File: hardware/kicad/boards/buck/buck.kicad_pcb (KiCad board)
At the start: 2 copper layers, 121 x 56 mm, 11 parts, among them J1 V1 ind (15V), J2 5V ud, J3 PWM (isoleret), J4 gate-forsyning, M1 IRF530N, U1 4N25

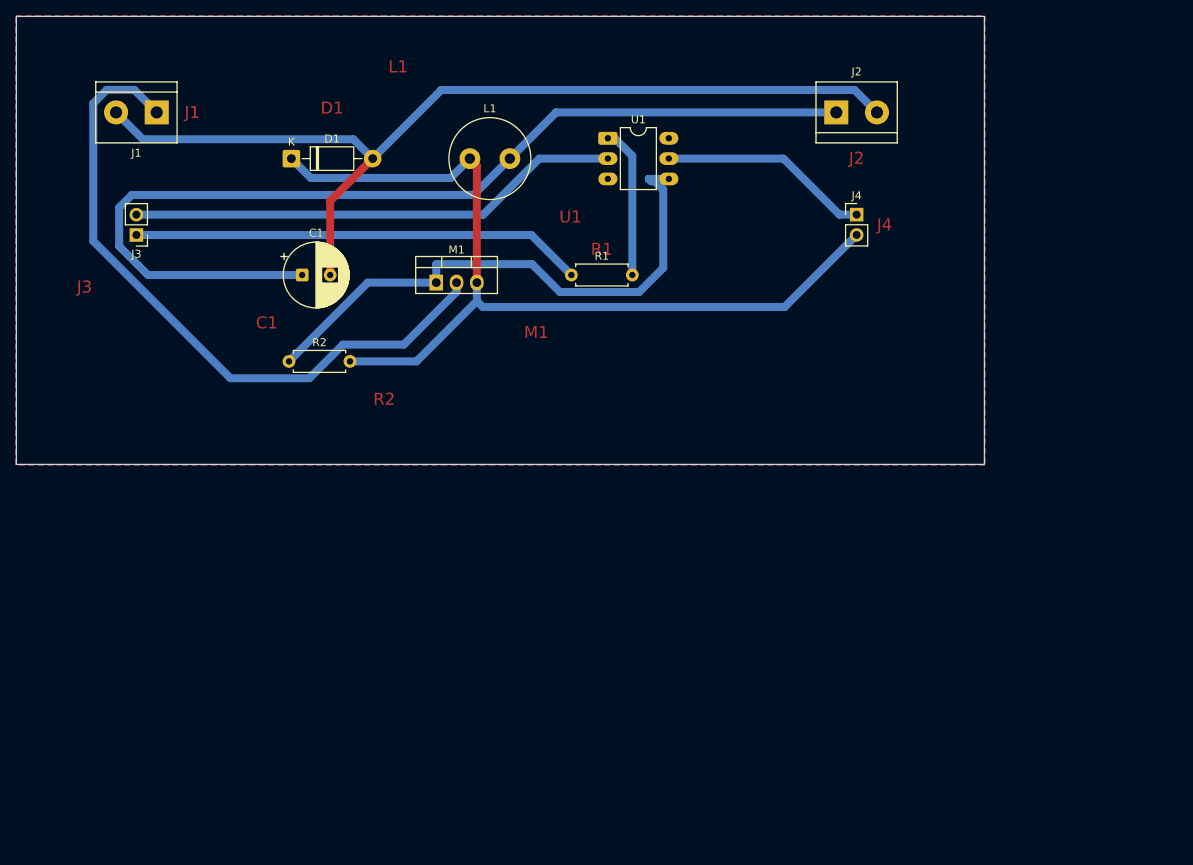
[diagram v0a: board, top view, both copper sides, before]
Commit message: Fit the measured 470uH toroid on buck/boost and fix the routing pipeline
L1 was placeholder Fastron 07P (D10/P5) - the wound toroid measures OD 34.5mm
standing on edge, legs 28.2mm c-c at 1.6mm dia. New footprint
energy_system:L_Toroid_Vertical_L34.5mm_W15.0mm_P28.20mm_LaserPads
(2.0mm drills, 4.0mm pads), boards regrown to 145x72 and rerouted
(buck 4 top tracks / boost only 2 now). Production DXF/gerbers re-exported.

Routing pipeline fixes that this flushed out:
- Set-Content -Encoding UTF8 under Windows PowerShell 5.1 writes a BOM and
  Freerouting's DSN parser chokes on it (bogus "file not found"). The stage-1
  mask now writes via [IO.File]::WriteAllText (BOM-less).
- Freerouting 2.0.1's version-check NPE can kill the SES save so jobs "hang"
  after routing; switched to the 1.9.0 jar (local CLI, same formats, Java 21).
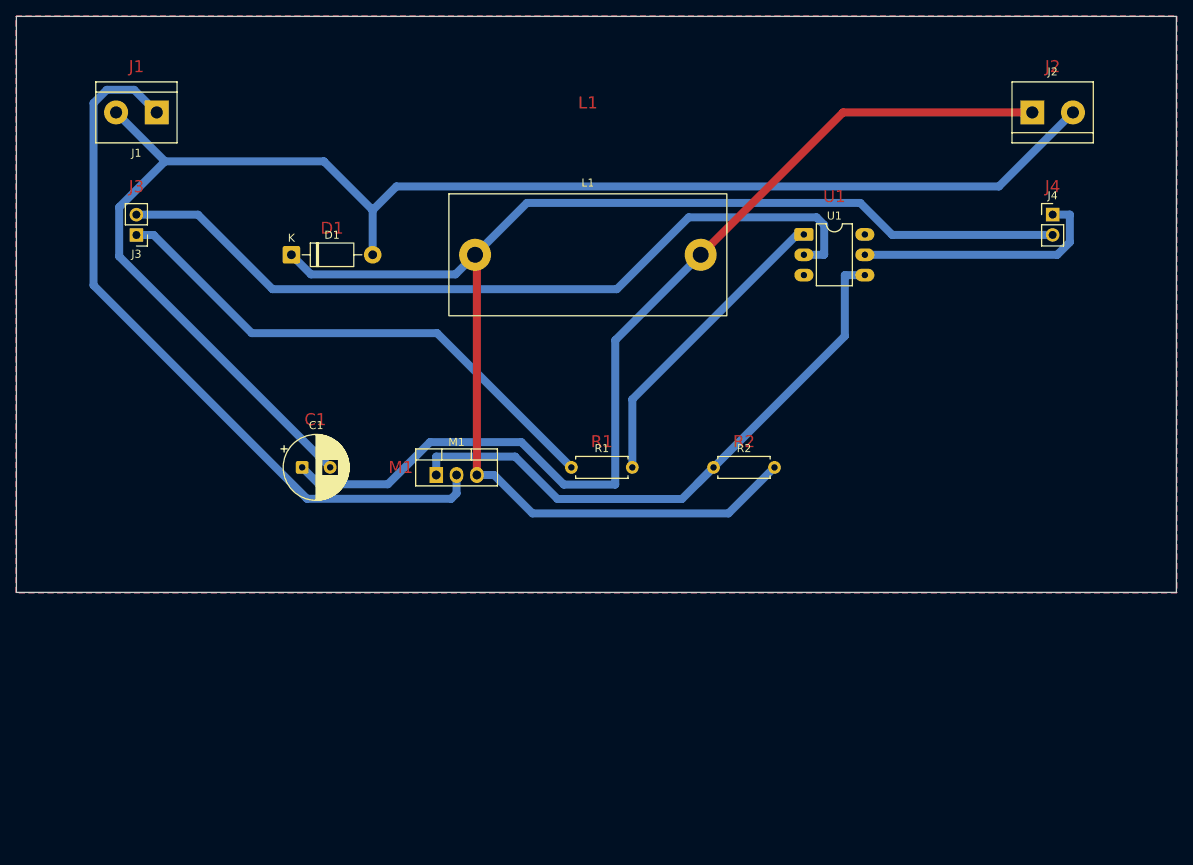
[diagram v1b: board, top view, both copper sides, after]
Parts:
- L1: footprint L_Radial_D10.0mm_P5.00mm_Fastron_07P -> L_Toroid_Vertical_L34.5mm_W15.0mm_P28.20mm_LaserPads
- moved R2 54.7 mm to (107.1, 76.4)
- moved U1 27.3 mm to (118.4, 47.3)
- moved J2 24.5 mm to (147.0, 32.0)
- moved J4 24.5 mm to (149.5, 44.8)
- moved M1 24.1 mm to (72.5, 77.3)
- moved C1 24.0 mm to (55.7, 76.4)
- moved R1 24.0 mm to (89.4, 76.4)
- moved L1 12.0 mm to (77.3, 49.8)
- moved D1 12.0 mm to (54.4, 49.8)
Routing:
- net /GND: track 119.0 -> 186.9 mm
- net /SW: track 113.0 -> 170.7 mm
- net GND_MCU: track 61.8 -> 100.2 mm
- net Net-(R1-Pad2): track 18.8 -> 38.5 mm
- net PWM: track 56.4 -> 66.4 mm
- net GATE: track 70.5 -> 76.9 mm
- net /VIN_15V: track 85.1 -> 91.5 mm
- net +12V_SW: track 26.4 -> 31.9 mm
- net /VOUT_5V: track 123.8 -> 126.4 mm
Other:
- board size 121 x 56 mm -> 145 x 72 mm

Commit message: Move all boards to the 104x104 jig format with compact placement
The laser positioning jig takes an exactly 109x109 mm copper blank, so every
board now has identical 104x104 edge cuts (2.5 mm rim). pcb_build.py:
- fixed JIG_W/JIG_H outline, hard failure if content overflows the square
- compact packing: 5 mm bbox gaps (was 8), squarish component cluster below
  the connector zone instead of full-width rows
- mppt/current_sense PLACE layouts re-arranged for the square and tightened

All 7 boards rerouted: 0 unconnected, 0 real DRC errors, and no vias needed
anywhere (the square format routes better than the old elongated boards).
Production DXF/gerbers re-exported; README run-plan updated for the jig
(cut blanks to exactly 109x109, all boards share the same size now).
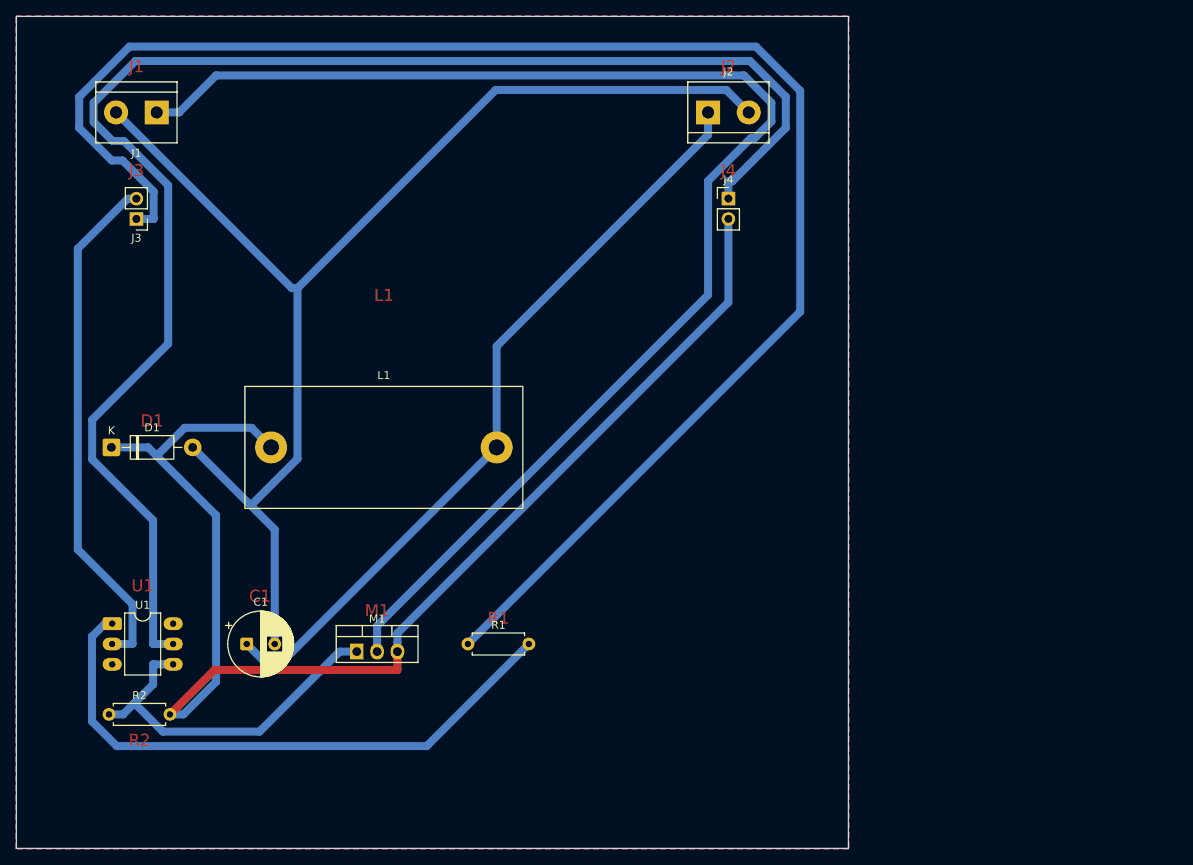
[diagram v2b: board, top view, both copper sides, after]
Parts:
- moved U1 99.2 mm to (32.0, 95.9)
- moved R2 81.6 mm to (31.6, 107.2)
- moved J4 40.6 mm to (109.0, 42.8)
- moved J2 40.5 mm to (106.5, 32.0)
- moved L1 35.1 mm to (51.8, 73.9)
- moved D1 33.0 mm to (31.9, 73.9)
- moved R1 25.6 mm to (76.4, 98.5)
- moved M1 24.2 mm to (62.5, 99.4)
- moved C1 23.1 mm to (48.8, 98.5)
- moved J3 2.00 mm to (35.0, 45.3)
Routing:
- net +12V_SW: track 31.9 -> 188.4 mm
- net PWM: track 66.4 -> 203.4 mm
- net /VIN_15V: track 91.5 -> 169.5 mm
- net Net-(R1-Pad2): track 38.5 -> 75.0 mm
- net GND_MCU: track 100.2 -> 64.7 mm
- net GATE: track 76.9 -> 45.5 mm
- net /VOUT_5V: track 126.4 -> 96.0 mm
- net /GND: track 186.9 -> 158.0 mm
- net /SW: track 170.7 -> 165.9 mm
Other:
- board size 145 x 72 mm -> 104 x 104 mm

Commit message: Condense and center all boards in the jig outline; reroute drive_circuit
Placement (pcb_build.py): connector columns now hug the component block
instead of sitting at the board edges, and the whole cluster is translated to
the center of the 104x104 outline - nothing sits next to the edge cuts
anymore. Fail-hard check if a cluster outgrows the jig.

drive_circuit keeps the hand-made GUI placement but is rerouted with the
two-stage flow: 43 top tracks + 1 via from the GUI autoroute down to 20
pin-to-pin bridges, no via. New tools/strip_routing.py removes existing
routing textually (sexpdata) - in-process pcbnew Remove() access-violates.

All 7 boards: 0 unconnected, 0 real DRC errors, no vias anywhere; buck is
now fully single-sided (0 top tracks). Production files re-exported.
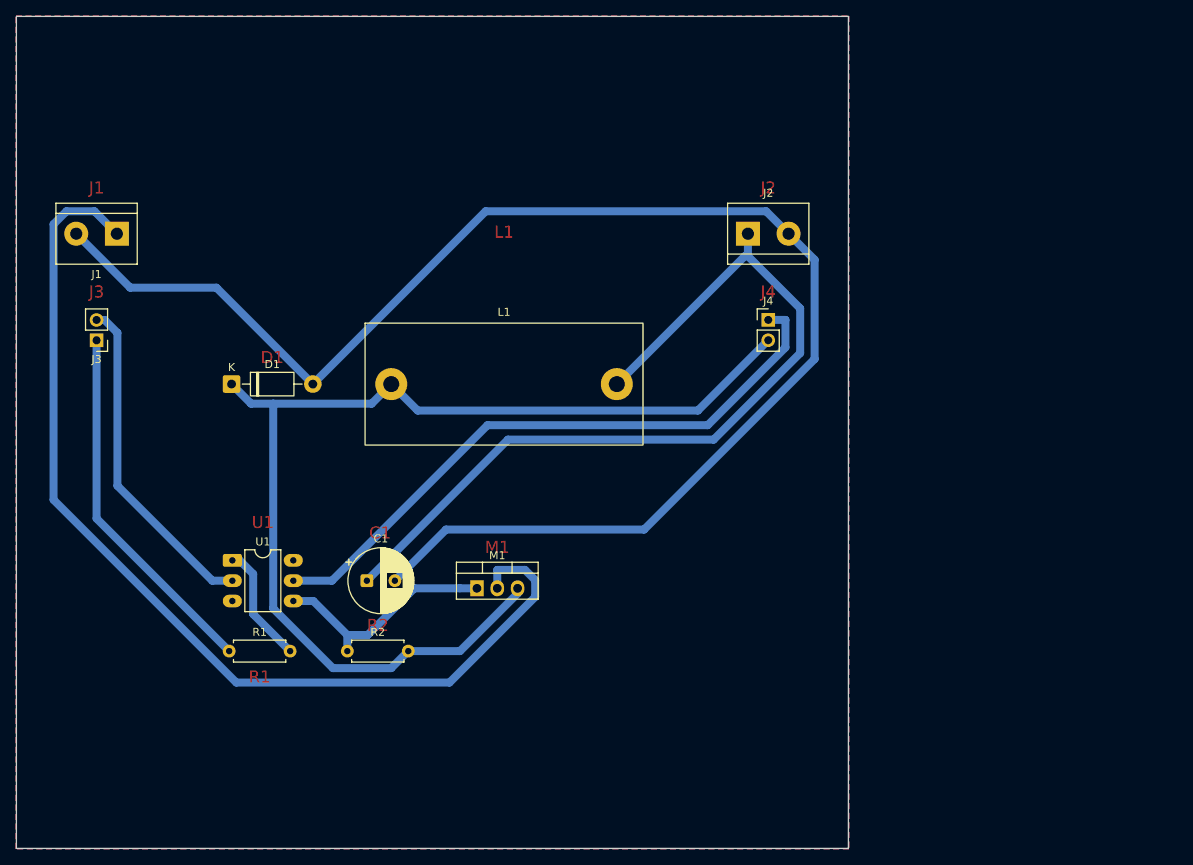
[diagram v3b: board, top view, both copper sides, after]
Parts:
- moved R2 30.8 mm to (61.4, 99.3)
- moved R1 29.9 mm to (46.6, 99.3)
- moved C1 17.0 mm to (63.8, 90.5)
- moved M1 17.0 mm to (77.6, 91.5)
- moved D1 17.0 mm to (46.9, 66.0)
- moved L1 17.0 mm to (66.9, 66.0)
- moved U1 17.0 mm to (47.0, 88.0)
- moved J2 16.0 mm to (111.4, 47.2)
- moved J4 16.0 mm to (114.0, 57.9)
- moved J1 16.0 mm to (32.6, 47.2)
- moved J3 16.0 mm to (30.0, 60.5)
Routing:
- net PWM: track 203.4 -> 45.7 mm
- net +12V_SW: track 188.4 -> 79.2 mm
- net Net-(R1-Pad2): track 75.0 -> 14.9 mm
- net /VIN_15V: track 169.5 -> 128.0 mm
- net /GND: track 158.0 -> 187.9 mm
- net /SW: track 165.9 -> 137.9 mm
- net GND_MCU: track 64.7 -> 41.7 mm
- net GATE: track 45.5 -> 29.1 mm
- net /VOUT_5V: track 96.0 -> 106.6 mm
